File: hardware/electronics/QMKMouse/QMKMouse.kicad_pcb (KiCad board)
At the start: 4 copper layers, 104.6 x 65.8 mm, 117 parts

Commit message: fix ERC errors and use hierarchy labels
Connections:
- net 1V8 renamed /MOS/1V8
- net 3V3 renamed /MCU/3V3
- net ButtonBack renamed /BTN/ButtonBack
- net ButtonDPI renamed /BTN/ButtonDPI
- net ButtonForward renamed /BTN/ButtonForward
- net ButtonLL renamed /BTN/ButtonLL
- net ButtonLeftClick renamed /BTN/ButtonLeftClick
- net ButtonRR renamed /BTN/ButtonRR
- net ButtonRightClick renamed /BTN/ButtonRightClick
- net ButtonScrollWheel renamed /BTN/ButtonScrollWheel
- net D+ renamed /MCU/D+
- net D- renamed /MCU/D-
- net LEDData renamed /LED/LEDData
- net MISO renamed /MCU/MISO
- net MOSI renamed /MCU/MOSI
- net MOTION renamed /MCU/MOTION
- net SCL renamed /MCU/SCL
- net SCLK renamed /MCU/SCLK
- net SDA renamed /MCU/SDA
- net TopScrollWheelOpto0 renamed /MCU/TopScrollWheelOpto0
- net TopScrollWheelOpto1 renamed /MCU/TopScrollWheelOpto1
- net V_USB renamed /LED/V_USB
- net ~{CS} renamed /MCU/~{CS}
- net ~{RESET} renamed /MCU/~{RESET}

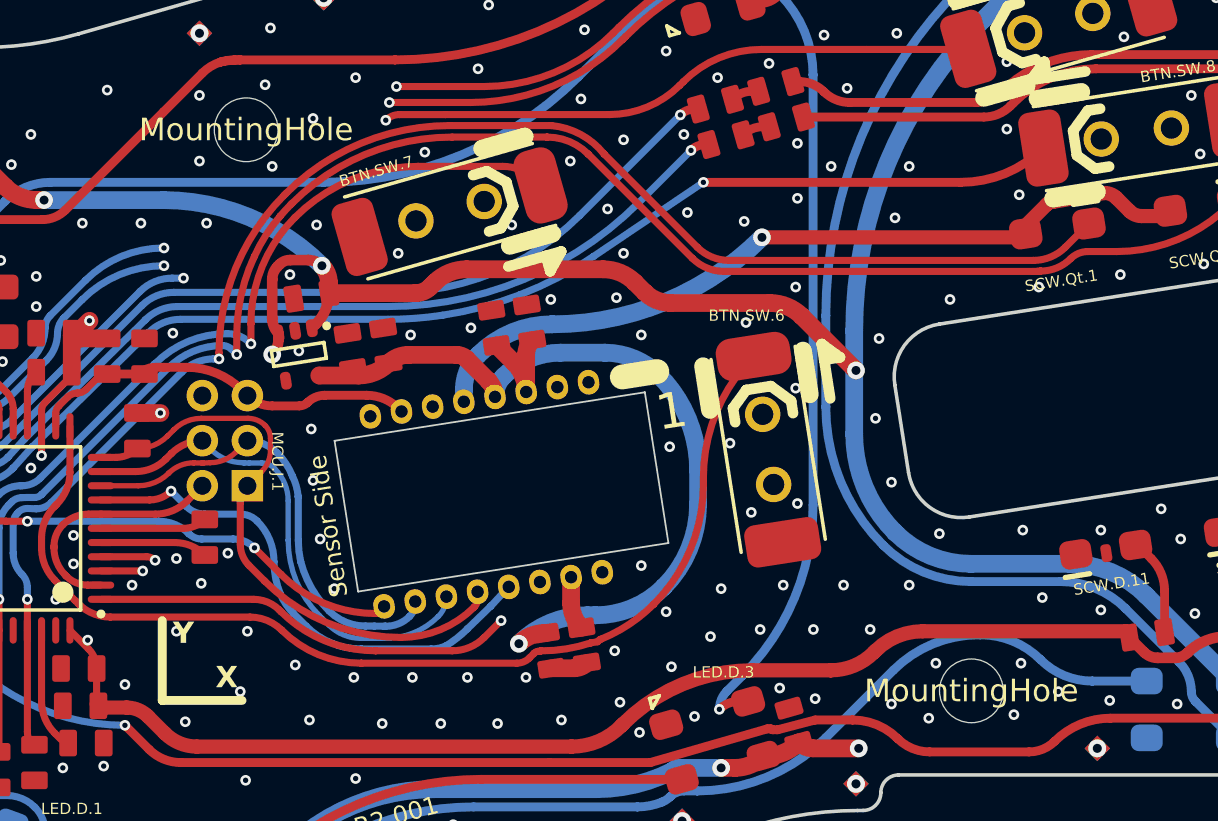
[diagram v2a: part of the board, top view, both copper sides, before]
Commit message: Fix capacitor value and streamline resistor value naming
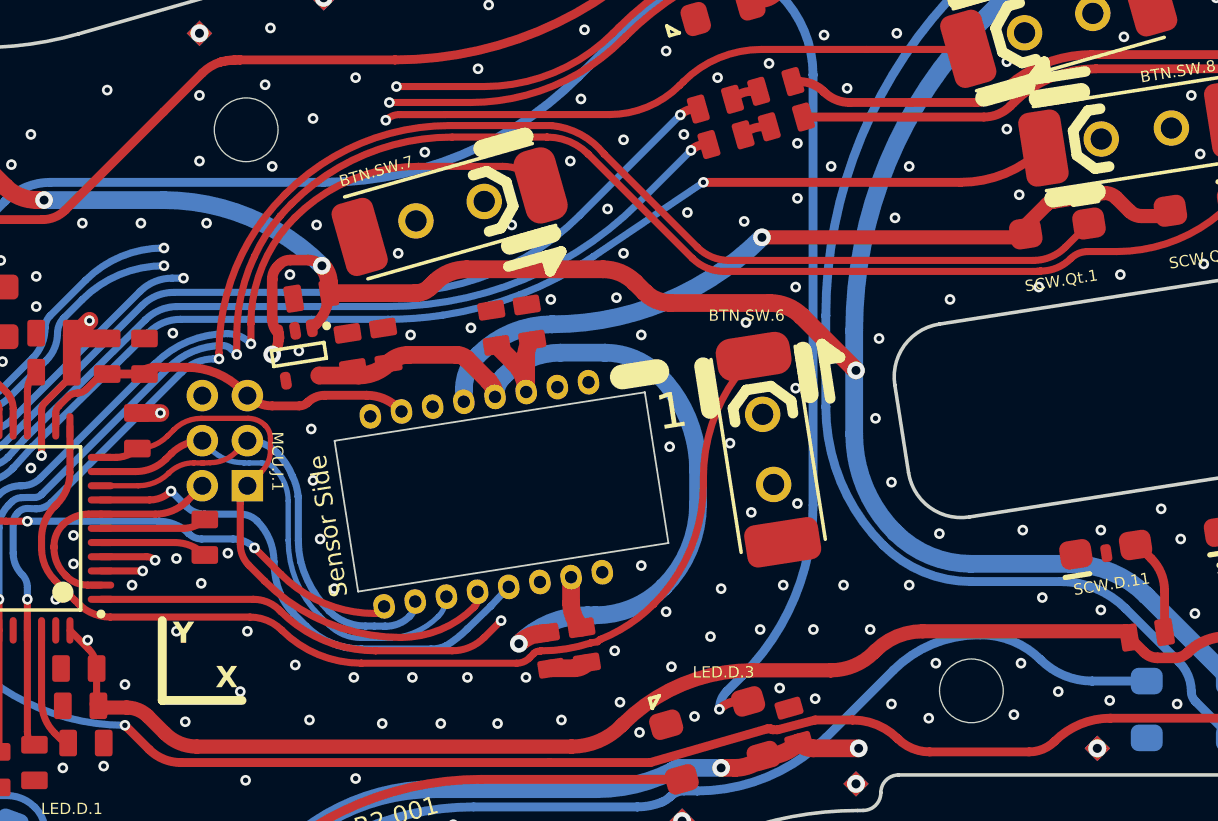
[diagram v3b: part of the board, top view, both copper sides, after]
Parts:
- MOS.C.11: value 10uF 25V -> 0.1uF 100V
- SCW.R.1, SCW.R.3: value 100 1% -> 100R 1%
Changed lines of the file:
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@@
       (effects (font (size 1.27 1.27) (thickness 0.15)))
     )
-    (fp_text value "MountingHole" (at 0 0) (layer "F.SilkS")
+    (fp_text value "MountingHole" (at 0 0) (layer "F.SilkS") hide
       (effects (font (size 1.27 1.27) (thickness 0.15)))
     )
@@
       (effects (font (size 0.635 0.635) (thickness 0.254)) (justify left bottom))
     )
-    (fp_text value "10uF 25V" (at -1.545668 3.061874 unlocked) (layer "F.SilkS") hide
+    (fp_text value "0.1uF 100V" (at -1.545668 3.061874 unlocked) (layer "F.SilkS") hide
       (effects (font (size 0.762 0.762) (thickness 0.254)) (justify left bottom))
     )
@@
       (effects (font (size 0.635 0.635) (thickness 0.254)) (justify left bottom))
     )
-    (fp_text value "100 1%" (at -1.545669 3.061876 unlocked) (layer "F.SilkS") hide
+    (fp_text value "100R 1%" (at -1.545669 3.061876 unlocked) (layer "F.SilkS") hide
       (effects (font (size 0.762 0.762) (thickness 0.254)) (justify left bottom))
     )
@@
       (effects (font (size 1.27 1.27) (thickness 0.15)))
     )
-    (fp_text value "MountingHole" (at 0 0) (layer "F.SilkS")
+    (fp_text value "MountingHole" (at 0 0) (layer "F.SilkS") hide
       (effects (font (size 1.27 1.27) (thickness 0.15)))
     )
@@
       (effects (font (size 0.635 0.635) (thickness 0.254)) (justify left bottom))
     )
-    (fp_text value "100 1%" (at 3.061875 1.545669 unlocked) (layer "F.SilkS") hide
-      (effects (font (size 0.762 0.762) (thickness 0.254)) (justify left bottom))
-    )
+    (fp_text value "100R 1%" (at 3.061875 1.545669 unlocked) (layer "F.SilkS") hide
+      (effects (font (size 0.762 0.762) (thickness 0.254)) (justify left bottom))
+    )

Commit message: fix minor Schematic naming errors; improve BoM generation
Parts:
- BTN.SW.7, BTN.SW.8: value SW_DIP_x01 -> D2LS-21
- LED.D.5: value Inolux_IN-PI554FCH -> IN-PI55TATPRPGPB
- USB.FB.4: value ACML-0805-601-T Ferrite Bead 600Ohm -> ACML-0805-601-T

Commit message: correct 2 resistor values and further improve BoM (BoM matches Altium BoM now)
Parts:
- USB.R.10, USB.R.11: value 100R 1% -> 22R 1%
